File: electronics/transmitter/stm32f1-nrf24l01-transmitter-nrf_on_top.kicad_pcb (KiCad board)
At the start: 2 copper layers, 24 parts, among them K1 CONN_3, K10 CONN_3, K11 CONN_3, K2 CONN_3, K3 CONN_3, K4 CONN_3, K5 CONN_3, K6 CONN_3, K7 CONN_3, K8 CONN_3, K9 CONN_3, P2 LED, P4 CONN_2, P5 CONN_4, Q1 BC548, U1 LIPO_CHARGER_+_PROTECTION, U2 STM32F103C8T6_DEV_BOARD, U3 NRF24L01P

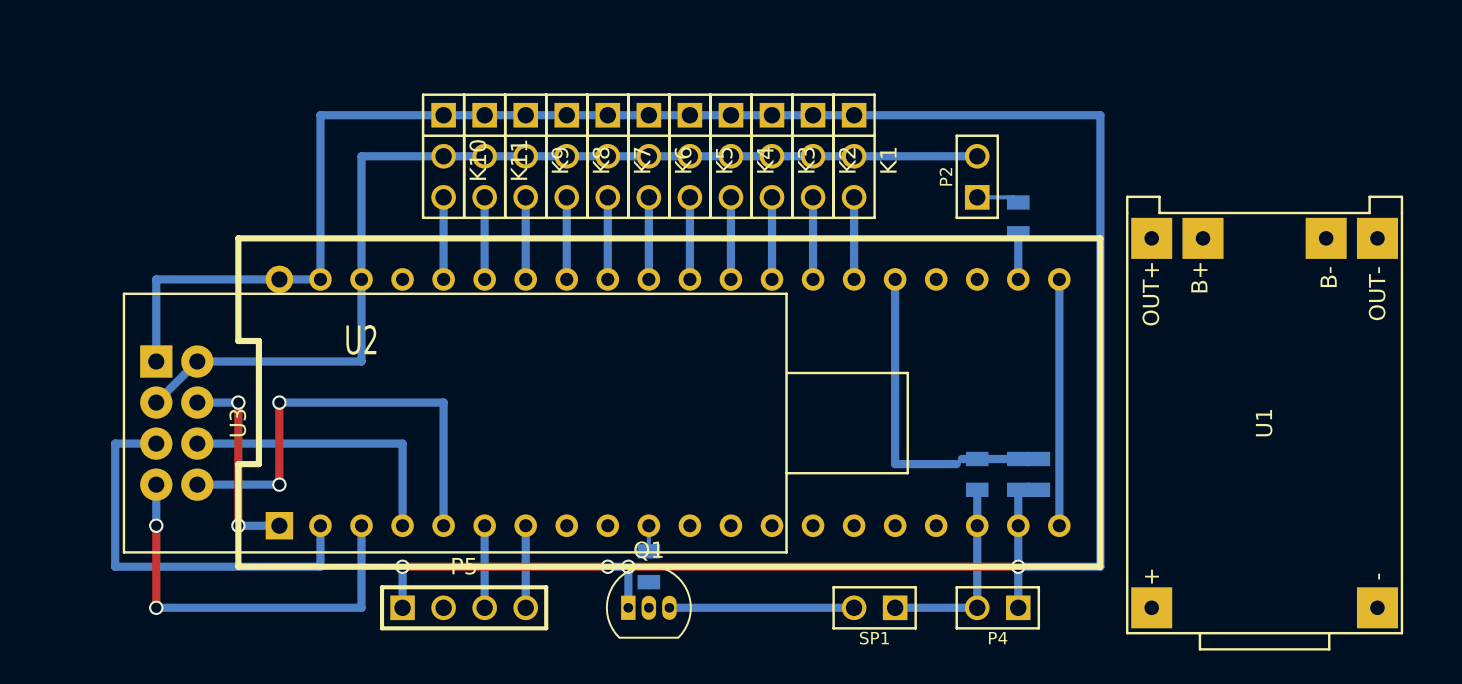
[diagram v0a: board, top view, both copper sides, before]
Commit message: Add buzzer and 3D images
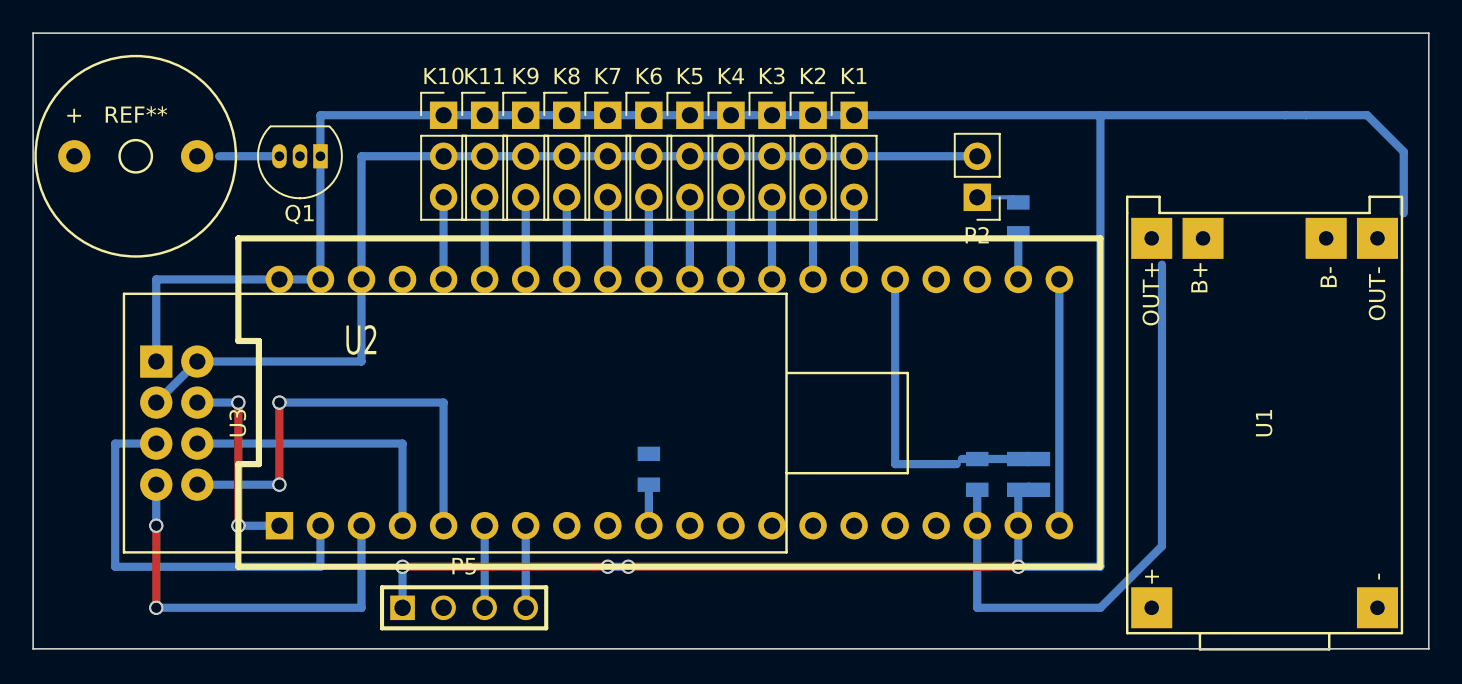
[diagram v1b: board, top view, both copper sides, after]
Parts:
- removed P4: CONN_2, PIN_ARRAY_2X1
- removed SP1: SPEAKER, PIN_ARRAY_2X1
- added REF**: Buzzer_12x9.5RM7.6, Buzzers_Beepers:Buzzer_12x9.5RM7.6, F.Cu at (217.2, 109.2)
- K1, K10, K11, K2, K3, K4, K5, K6, K7, K8, K9: footprint PIN_ARRAY_3X1 -> Pin_Headers:Pin_Header_Straight_1x03_Pitch2.54mm
- P2: footprint PIN_ARRAY_2X1 -> Pin_Headers:Pin_Header_Straight_1x02_Pitch2.54mm
- U1: footprint LiPo_charger_and_protection -> WLA:LiPo_charger_and_protection
- U2: footprint WLA-STM32:STM32F103C8T6 -> WLA:STM32F103C8T6
- U3: footprint NRF24L01P-PA-LNA -> WLA:NRF24L01P-PA-LNA
- moved Q1 33.8 mm to (228.6, 109.2), turned to 180 degrees
- moved R4 6.03 mm to (248.9, 128.6), turned to 90 degrees
- moved K1 2.54 mm to (261.6, 106.7), turned to 0 degrees
- moved K10 2.54 mm to (236.2, 106.7), turned to 0 degrees
- moved K11 2.54 mm to (238.8, 106.7), turned to 0 degrees
- moved K2 2.54 mm to (259.1, 106.7), turned to 0 degrees
- moved K3 2.54 mm to (256.5, 106.7), turned to 0 degrees
- moved K4 2.54 mm to (254.0, 106.7), turned to 0 degrees
- moved K5 2.54 mm to (251.5, 106.7), turned to 0 degrees
- moved K6 2.54 mm to (248.9, 106.7), turned to 0 degrees
- moved K7 2.54 mm to (246.4, 106.7), turned to 0 degrees
- moved K8 2.54 mm to (243.8, 106.7), turned to 0 degrees
- moved K9 2.54 mm to (241.3, 106.7), turned to 0 degrees
- moved P2 1.27 mm to (269.2, 111.8), turned to 180 degrees
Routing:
- net VDD: track 12.4 -> 37.7 mm
- net GND: track 158.4 -> 176.9 mm
- net N-0000014: track 11.4 -> 3.73 mm
- net /BUZZER: track 1.59 -> 2.54 mm
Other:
- board outline added: 86.4 x 38.1 mm
